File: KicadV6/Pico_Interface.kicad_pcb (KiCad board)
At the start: 2 copper layers, 42.5 x 40.6 mm, 3 parts, among them J1 Conn_02x05_Odd_Even, J2 Conn_01x03_Male, U1 Pico

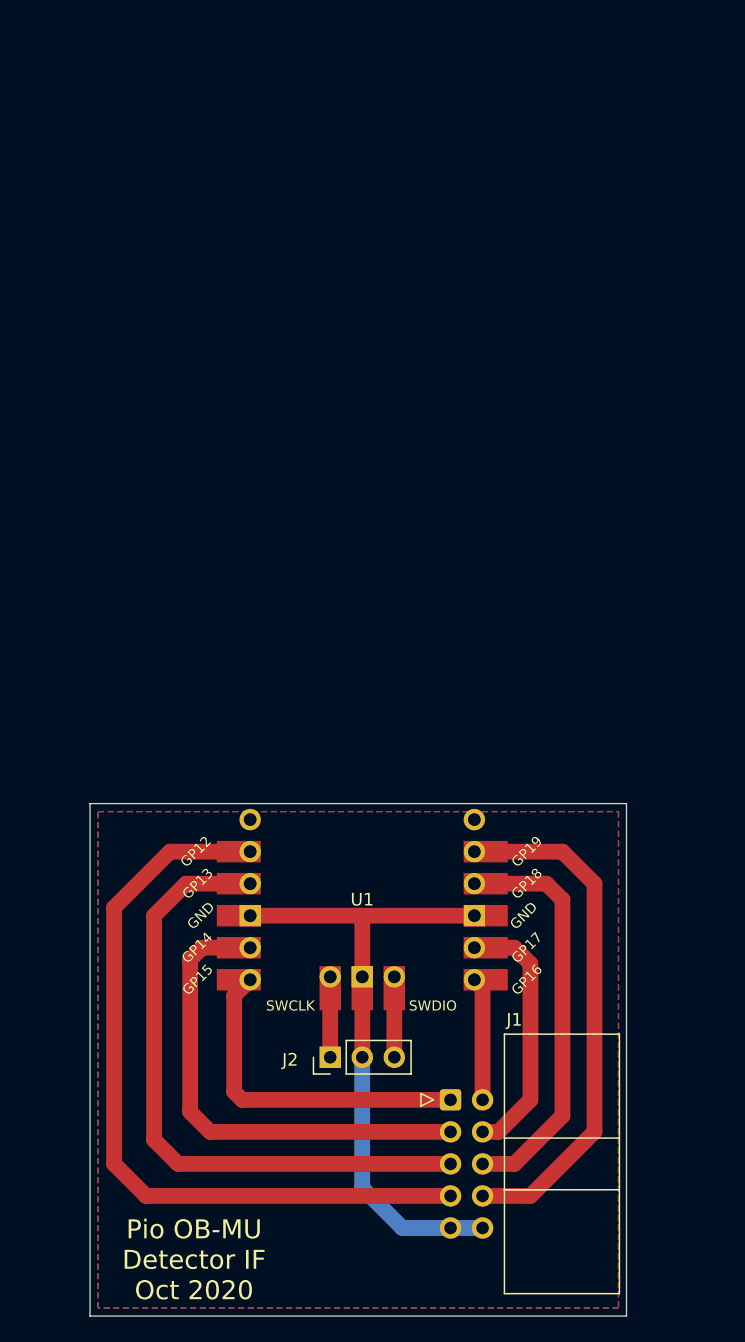
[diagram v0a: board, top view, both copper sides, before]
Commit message: Added 4 PMOD / IDC Connectors
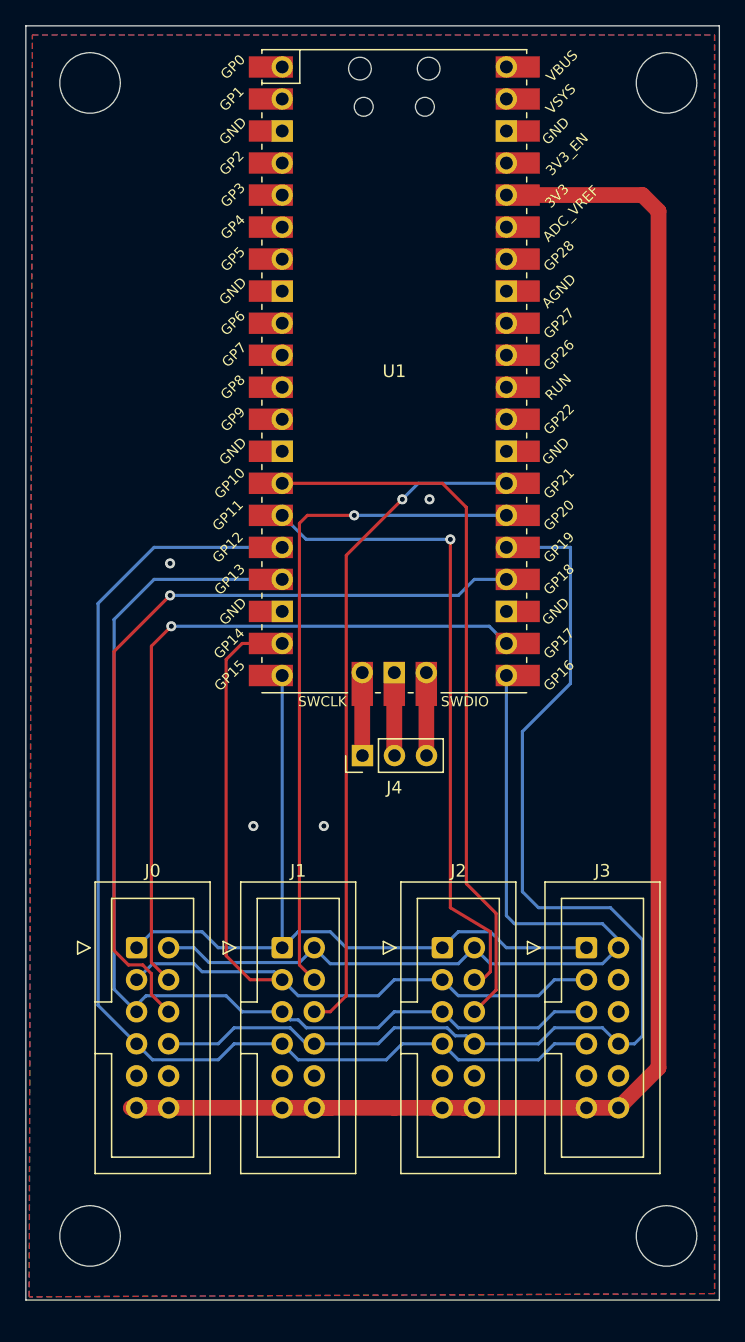
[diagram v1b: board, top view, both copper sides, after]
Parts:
- added J0: Conn_02x06_Odd_Even, Connector_IDC:IDC-Header_2x06_P2.54mm_Vertical, F.Cu at (88.8, 118.1)
- added J3: Conn_02x06_Odd_Even, Connector_IDC:IDC-Header_2x06_P2.54mm_Vertical, F.Cu at (124.5, 118.1)
- added J4: Conn_01x03_Male, Connector_PinHeader_2.54mm:PinHeader_1x03_P2.54mm_Vertical, F.Cu at (106.7, 102.9)
- J1: value Conn_02x05_Odd_Even -> Conn_02x06_Odd_Even; footprint Connector_IDC:IDC-Header_2x05_P2.54mm_Horizontal -> Connector_IDC:IDC-Header_2x06_P2.54mm_Vertical
- J2: value Conn_01x03_Male -> Conn_02x06_Odd_Even; footprint Connector_PinHeader_2.54mm:PinHeader_1x03_P2.54mm_Vertical -> Connector_IDC:IDC-Header_2x06_P2.54mm_Vertical
- U1: footprint MCU_RaspberryPi_and_Boards:RPi_Pico_SMD_TH_PART -> RPi_Pico:RPi_Pico_SMD_TH
- moved U1 24.3 mm to (109.2, 72.4)
- moved J1 18.0 mm to (100.3, 118.1)
- moved J2 12.4 mm to (113.0, 118.1), turned to 0 degrees
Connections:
- J1 pad 1: Net-(U1-Pad20) -> /DVDD_EN
- J1 pad 2: Net-(U1-Pad21) -> /AVDD_EN
- J1 pad 3: Net-(U1-Pad19) -> /MCLK_O
- J1 pad 4: Net-(U1-Pad22) -> /DCTRL_O_1
- J1 pad 5: Net-(U1-Pad17) -> /MCLK_I
- J1 pad 6: Net-(U1-Pad24) -> /DCTRL_I_1
- J1 pad 7: Net-(U1-Pad16) -> /MCLK_OE
- J1 pad 8: Net-(U1-Pad25) -> /DCTRL_OE
- J2 pad 1: Net-(U1-Pad41) -> /DVDD_EN
- J2 pad 2: GND -> /AVDD_EN
- J2 pad 3: Net-(U1-Pad43) -> /MCLK_O
- U1 pad 15: unconnected-(U1-Pad15) -> /DCTRL_O_2
- U1 pad 16: Net-(U1-Pad16) -> /MCLK_OE
- U1 pad 17: Net-(U1-Pad17) -> /MCLK_I
- U1 pad 19: Net-(U1-Pad19) -> /MCLK_O
- U1 pad 20: Net-(U1-Pad20) -> /DVDD_EN
- U1 pad 21: Net-(U1-Pad21) -> /AVDD_EN
- U1 pad 22: Net-(U1-Pad22) -> /DCTRL_O_0
- U1 pad 24: Net-(U1-Pad24) -> /DCTRL_I_0
- U1 pad 25: Net-(U1-Pad25) -> /DCTRL_OE
- U1 pad 26: unconnected-(U1-Pad26) -> /DCTRL_O_1
- U1 pad 41: Net-(U1-Pad41) -> Net-(J4-Pad1)
- U1 pad 43: Net-(U1-Pad43) -> Net-(J4-Pad3)
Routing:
- net +3.3V: track 0.00 -> 124.8 mm
- net /DCTRL_OE: track 0.00 -> 93.7 mm
- net /MCLK_OE: track 0.00 -> 92.0 mm
- net /MCLK_I: track 0.00 -> 85.6 mm
- net /MCLK_O: track 0.00 -> 72.5 mm
- net /AVDD_EN: track 0.00 -> 68.1 mm
- net /DCTRL_I_0: track 0.00 -> 64.5 mm, vias 0 -> 1
- net Net-(U1-Pad16): track 60.7 -> 0.00 mm
- net /DVDD_EN: track 0.00 -> 60.4 mm
- net /DCTRL_I_2: track 0.00 -> 57.1 mm
- net /DCTRL_O_0: track 0.00 -> 56.5 mm, vias 0 -> 1
- net /DCTRL_O_1: track 0.00 -> 53.4 mm, vias 0 -> 1
- net /DCTRL_I_1: track 0.00 -> 53.1 mm, vias 0 -> 1
- net /DCTRL_O_2: track 0.00 -> 51.7 mm, vias 0 -> 1
- net Net-(U1-Pad17): track 50.8 -> 0.00 mm
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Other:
- board size 42.5 x 40.6 mm -> 55 x 101.1 mm
- board text removed: "Pio OB-MU Detector IF Oct 2020"

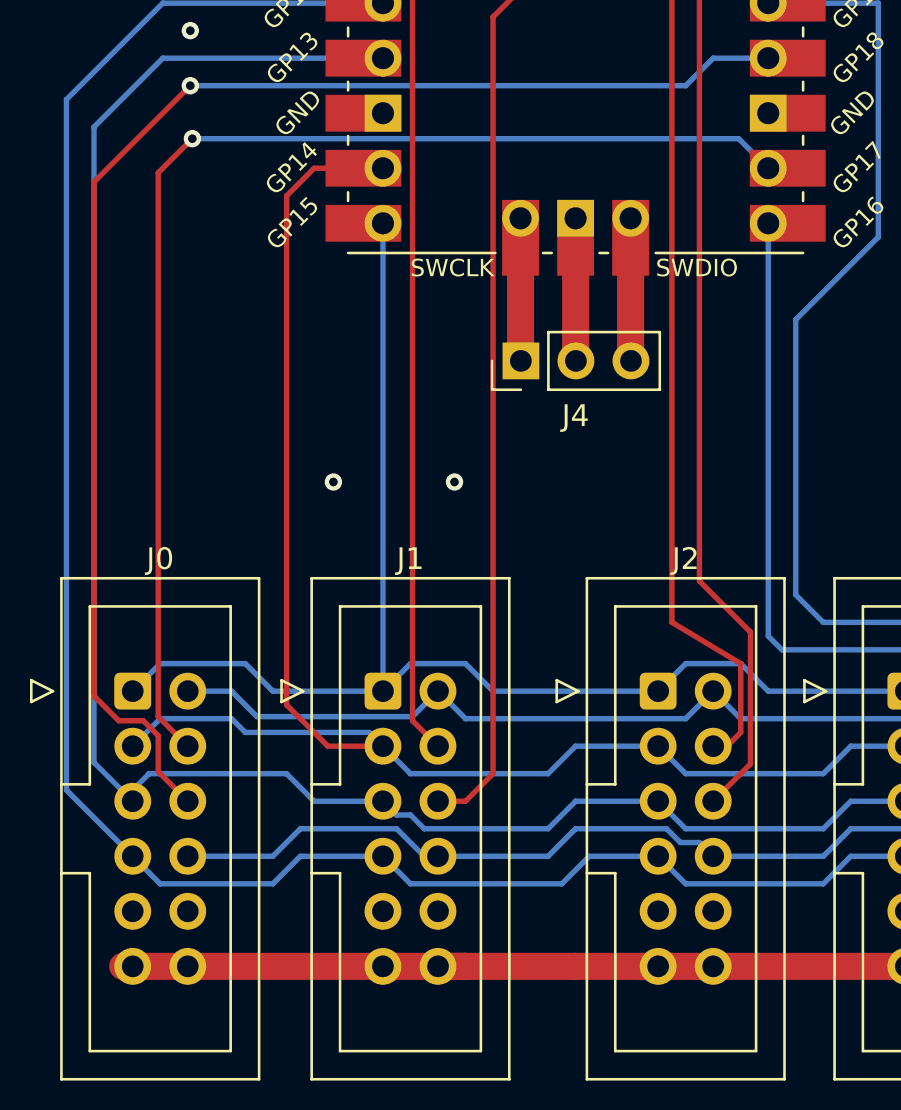
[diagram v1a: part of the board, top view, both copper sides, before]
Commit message: DRC Warning fix
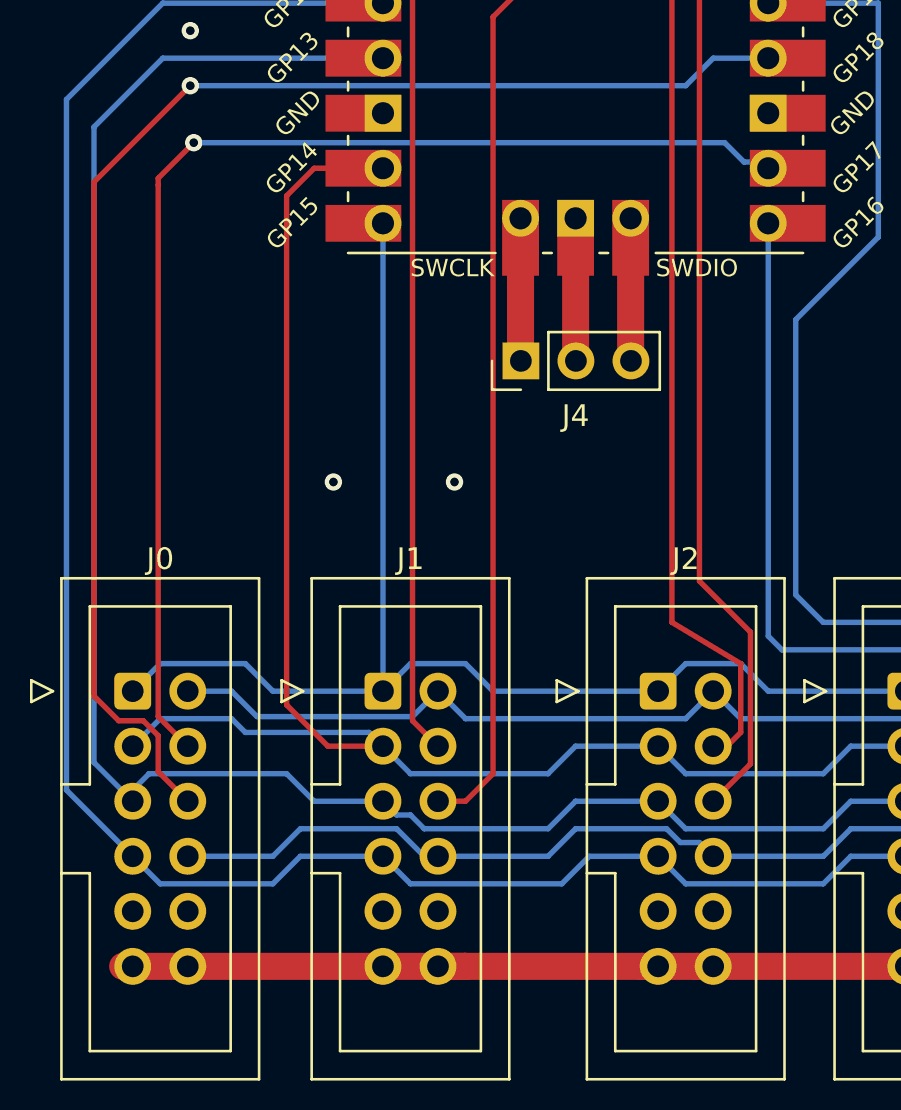
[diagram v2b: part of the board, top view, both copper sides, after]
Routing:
- net /MCLK_OE: track 92.0 -> 91.5 mm
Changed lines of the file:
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@@
   (segment (start 107.95 121.92) (end 109.22 120.65) (width 0.25) (layer "B.Cu") (net 5))
   (segment (start 109.22 120.65) (end 113.03 120.65) (width 0.25) (layer "B.Cu") (net 5))
-  (segment (start 89.9575 94.1925) (end 89.9575 119.285) (width 0.25) (layer "F.Cu") (net 6))
-  (segment (start 91.535 92.615) (end 89.9575 94.1925) (width 0.25) (layer "F.Cu") (net 6))
+  (segment (start 89.9575 94.7575) (end 89.9575 119.285) (width 0.25) (layer "F.Cu") (net 6))
+  (segment (start 91.6 92.8) (end 89.9575 94.4425) (width 0.25) (layer "F.Cu") (net 6))
   (segment (start 89.9575 119.285) (end 91.3225 120.65) (width 0.25) (layer "F.Cu") (net 6))
-  (via (at 91.535 92.615) (size 0.8) (drill 0.4) (layers "F.Cu" "B.Cu") (net 6))
-  (segment (start 116.745 92.615) (end 91.535 92.615) (width 0.25) (layer "B.Cu") (net 6))
-  (segment (start 91.44 92.71) (end 91.535 92.615) (width 0.25) (layer "B.Cu") (net 6))
-  (segment (start 118.11 93.98) (end 116.745 92.615) (width 0.25) (layer "B.Cu") (net 6))
+  (segment (start 89.9575 94.4425) (end 89.9575 94.7575) (width 0.25) (layer "F.Cu") (net 6))
+  (via (at 91.6 92.8) (size 0.8) (drill 0.4) (layers "F.Cu" "B.Cu") (net 6))
+  (segment (start 91.6 92.8) (end 116.1 92.8) (width 0.25) (layer "B.Cu") (net 6))
+  (segment (start 117.825 93.695) (end 118.11 93.98) (width 0.25) (layer "B.Cu") (net 6))
+  (segment (start 116.995 93.695) (end 117.825 93.695) (width 0.25) (layer "B.Cu") (net 6))
+  (segment (start 116.1 92.8) (end 116.995 93.695) (width 0.25) (layer "B.Cu") (net 6))
   (segment (start 95.885 121.92) (end 97.155 123.19) (width 0.25) (layer "B.Cu") (net 7))
   (segment (start 113.03 123.19) (end 114.3 124.46) (width 0.25) (layer "B.Cu") (net 7))
@@
   (segment (start 88.7825 125.73) (end 90.0525 127) (width 0.25) (layer "B.Cu") (net 9))
   (segment (start 121.92 125.73) (end 124.46 125.73) (width 0.25) (layer "B.Cu") (net 9))
-  (segment (start 88.7825 125.73) (end 88.7825 125.2125) (width 0.25) (layer "B.Cu") (net 9))
   (segment (start 95.25 127) (end 96.52 125.73) (width 0.25) (layer "B.Cu") (net 9))
   (segment (start 120.65 127) (end 121.92 125.73) (width 0.25) (layer "B.Cu") (net 9))
@@
   (segment (start 100.2975 130.81) (end 90.8575 130.81) (width 1.25) (layer "F.Cu") (net 12))
   (segment (start 90.8575 130.81) (end 88.3175 130.81) (width 1.25) (layer "F.Cu") (net 12))
-  (segment (start 109.22 130.81) (end 104.14 130.81) (width 1.25) (layer "F.Cu") (net 12))
+  (segment (start 104.14 130.81) (end 112.2775 130.81) (width 1.25) (layer "F.Cu") (net 12))
   (segment (start 124.2575 130.81) (end 126.7975 130.81) (width 1.25) (layer "F.Cu") (net 12))
   (segment (start 104.14 130.81) (end 100.2975 130.81) (width 1.25) (layer "F.Cu") (net 12))
@@
   (segment (start 114.8175 130.81) (end 124.2575 130.81) (width 1.25) (layer "F.Cu") (net 12))
   (segment (start 104.14 130.81) (end 102.8375 130.81) (width 1.25) (layer "F.Cu") (net 12))
-  (segment (start 109.22 130.81) (end 112.2775 130.81) (width 1.25) (layer "F.Cu") (net 12))
   (segment (start 101.695 119.475) (end 102.87 120.65) (width 0.25) (layer "F.Cu") (net 13))
   (segment (start 106.045 83.82) (end 102.33 83.82) (width 0.25) (layer "F.Cu") (net 13))
